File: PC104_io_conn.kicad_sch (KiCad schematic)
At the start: 14 parts, among them J13 ESQ-126-39-G-D_SAI, J15 ESQ-126-39-G-D_SAI

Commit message: A bunch of work on component selections
And little fixups for things I found.

Signed-off-by: Corey Minyard <corey@minyard.net>
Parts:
- C114, C133: value 10uF 10v -> 10uF 10V
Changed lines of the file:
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@@
 			)
 		)
-		(property "Value" "10uF 10v"
+		(property "Value" "10uF 10V"
 			(at 168.529 185.293 0)
 			(effects
@@
 			)
 		)
-		(property "Value" "10uF 10v"
+		(property "Value" "10uF 10V"
 			(at 88.011 162.433 0)
 			(effects

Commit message: More minor part number updates
Signed-off-by: Corey Minyard <corey@minyard.net>
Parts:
- J13, J15: value ESQ-126-39-G-D_SAI -> ESQ-126-39-G-D
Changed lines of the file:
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@@
 			)
 		)
-		(property "Value" "ESQ-126-39-G-D_SAI"
+		(property "Value" "ESQ-126-39-G-D"
 			(at 144.78 92.71 0)
 			(effects
@@
 			)
 		)
-		(property "Value" "ESQ-126-39-G-D_SAI"
+		(property "Value" "ESQ-126-39-G-D"
 			(at 248.92 92.71 0)
 			(effects

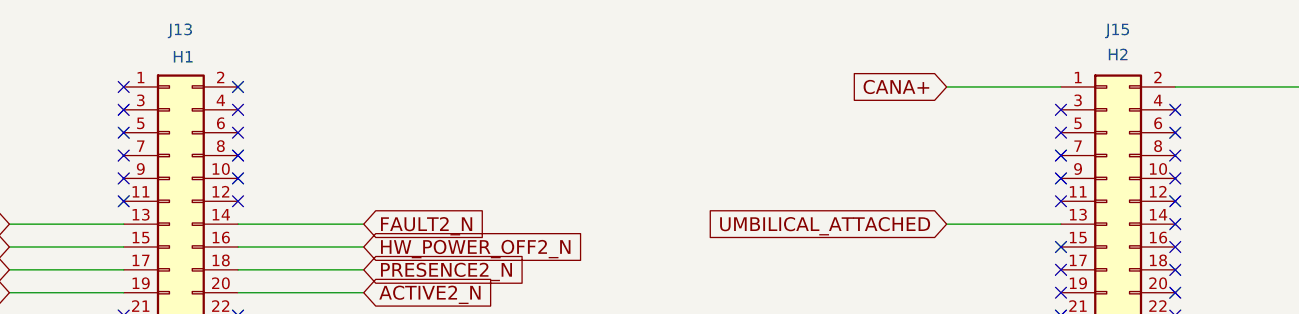
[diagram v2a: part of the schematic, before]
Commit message: Renumber shields and PC104 sockets
Separate out shields into their own designator category.

Make the PC104 sockets J1 and J2 to make it easier to move to other
boards.

Signed-off-by: Corey Minyard <corey@minyard.net>
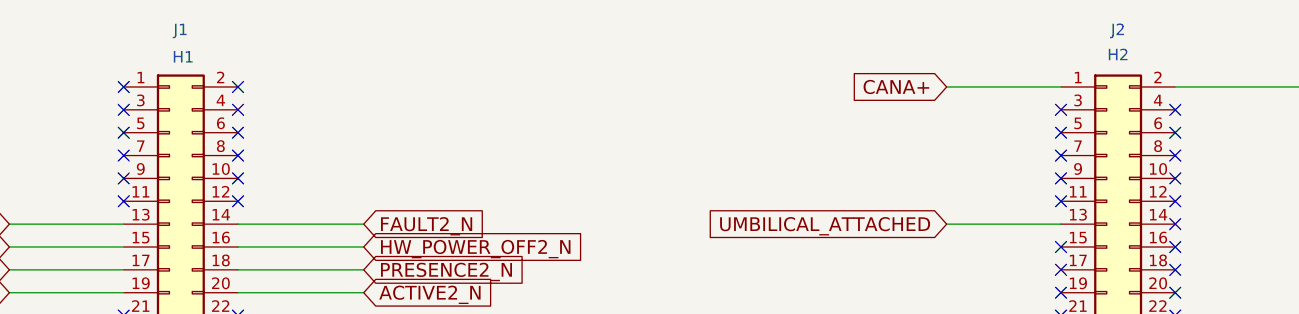
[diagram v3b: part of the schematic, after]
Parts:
- renumbered J13 to J1, J15 to J2
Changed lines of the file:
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@@
 		(on_board yes)
 		(dnp no)
-		(property "Reference" "J13"
+		(property "Reference" "J1"
 			(at 144.78 90.17 0)
 			(effects
@@
 			(project ""
 				(path "/cc9f42d2-6985-41ac-acab-5ab7b01c5b38/163b95be-82a7-4cd3-9077-48a01f79e25c"
-					(reference "J13")
+					(reference "J1")
 					(unit 1)
 				)
@@
 		(on_board yes)
 		(dnp no)
-		(property "Reference" "J15"
+		(property "Reference" "J2"
 			(at 248.92 90.17 0)
 			(effects
@@
 			(project "PacSat_AFSK"
 				(path "/cc9f42d2-6985-41ac-acab-5ab7b01c5b38/163b95be-82a7-4cd3-9077-48a01f79e25c"
-					(reference "J15")
+					(reference "J2")
 					(unit 1)
 				)

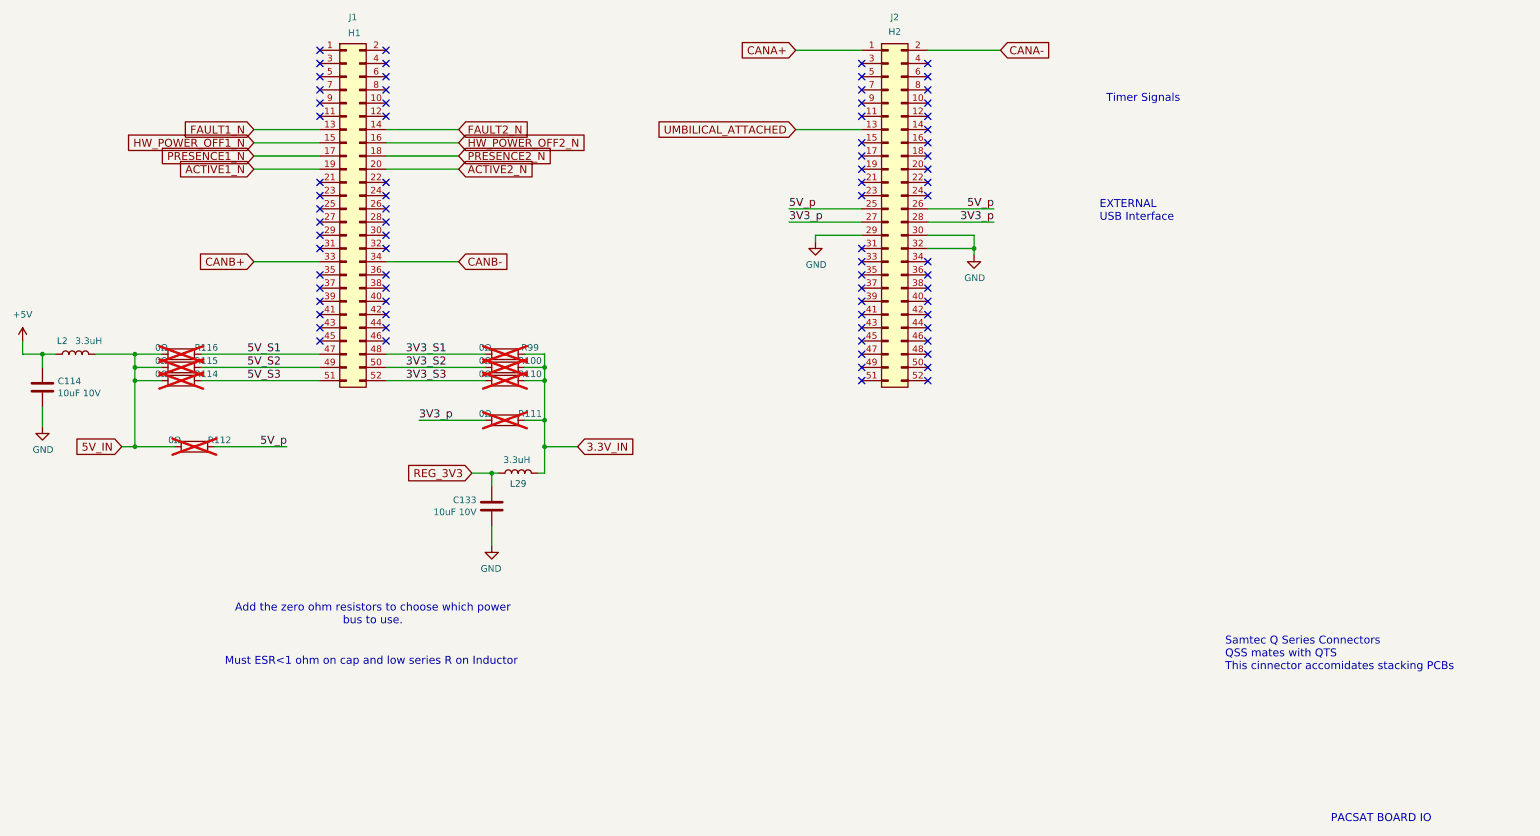
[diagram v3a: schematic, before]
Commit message: Rework the board to be the Fox Plus setup
Signed-off-by: Corey Minyard <corey@minyard.net>
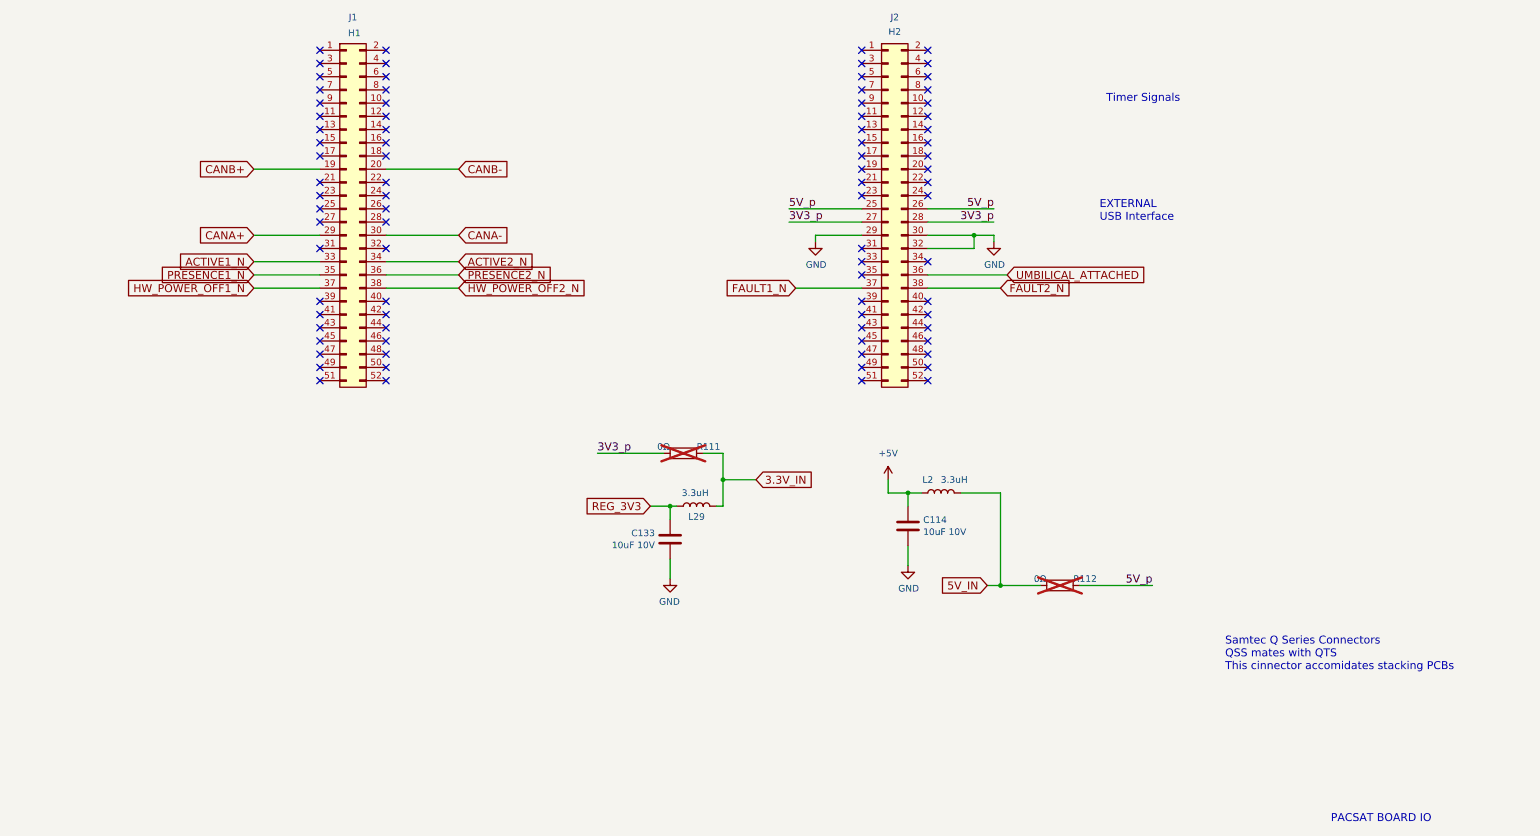
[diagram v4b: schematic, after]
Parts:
- removed R100, R110, R114, R115, R116, R99: 0Ω, Resistor_SMD:R_0603_1608Metric_Pad0.98x0.95mm_HandSolder, symbol Device:R
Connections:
- net ACTIVE1_N: now also J1.33 (Pin_33); no longer J1.19 (Pin_19)
- net ACTIVE2_N: now also J1.34 (Pin_34); no longer J1.20 (Pin_20)
- net CANA+: now also J1.29 (Pin_29); no longer J2.1 (Pin_1)
- net CANA-: now also J1.30 (Pin_30); no longer J2.2 (Pin_2)
- net CANB+: now also J1.19 (Pin_19); no longer J1.33 (Pin_33)
- net CANB-: now also J1.20 (Pin_20); no longer J1.34 (Pin_34)
- net FAULT1_N: now also J2.37 (Pin_37); no longer J1.13 (Pin_13)
- net FAULT2_N: now also J2.38 (Pin_38); no longer J1.14 (Pin_14)
- net HW_POWER_OFF1_N: now also J1.37 (Pin_37); no longer J1.15 (Pin_15)
- net HW_POWER_OFF2_N: now also J1.38 (Pin_38); no longer J1.16 (Pin_16)
- net PRESENCE1_N: now also J1.35 (Pin_35); no longer J1.17 (Pin_17)
- net PRESENCE2_N: now also J1.36 (Pin_36); no longer J1.18 (Pin_18)
- net UMBILICAL_ATTACHED: now also J2.36 (Pin_36); no longer J2.13 (Pin_13)
- net 3V3_S1: no longer names the net of J1.48 (Pin_48)
- net 3V3_S2: no longer names the net of J1.50 (Pin_50)
- net 3V3_S3: no longer names the net of J1.52 (Pin_52)
- net 5V_S1: no longer names the net of J1.47 (Pin_47)
- net 5V_S2: no longer names the net of J1.49 (Pin_49)
- net 5V_S3: no longer names the net of J1.51 (Pin_51)
- no-connect marks 78 -> 84
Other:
- note removed: "Add the zero ohm resistors to choose which power bus to use."
- note removed: "Must ESR<1 ohm on cap and low series R on Inductor"
- moved on the sheet: C114, C133, L2, L29, R111, R112

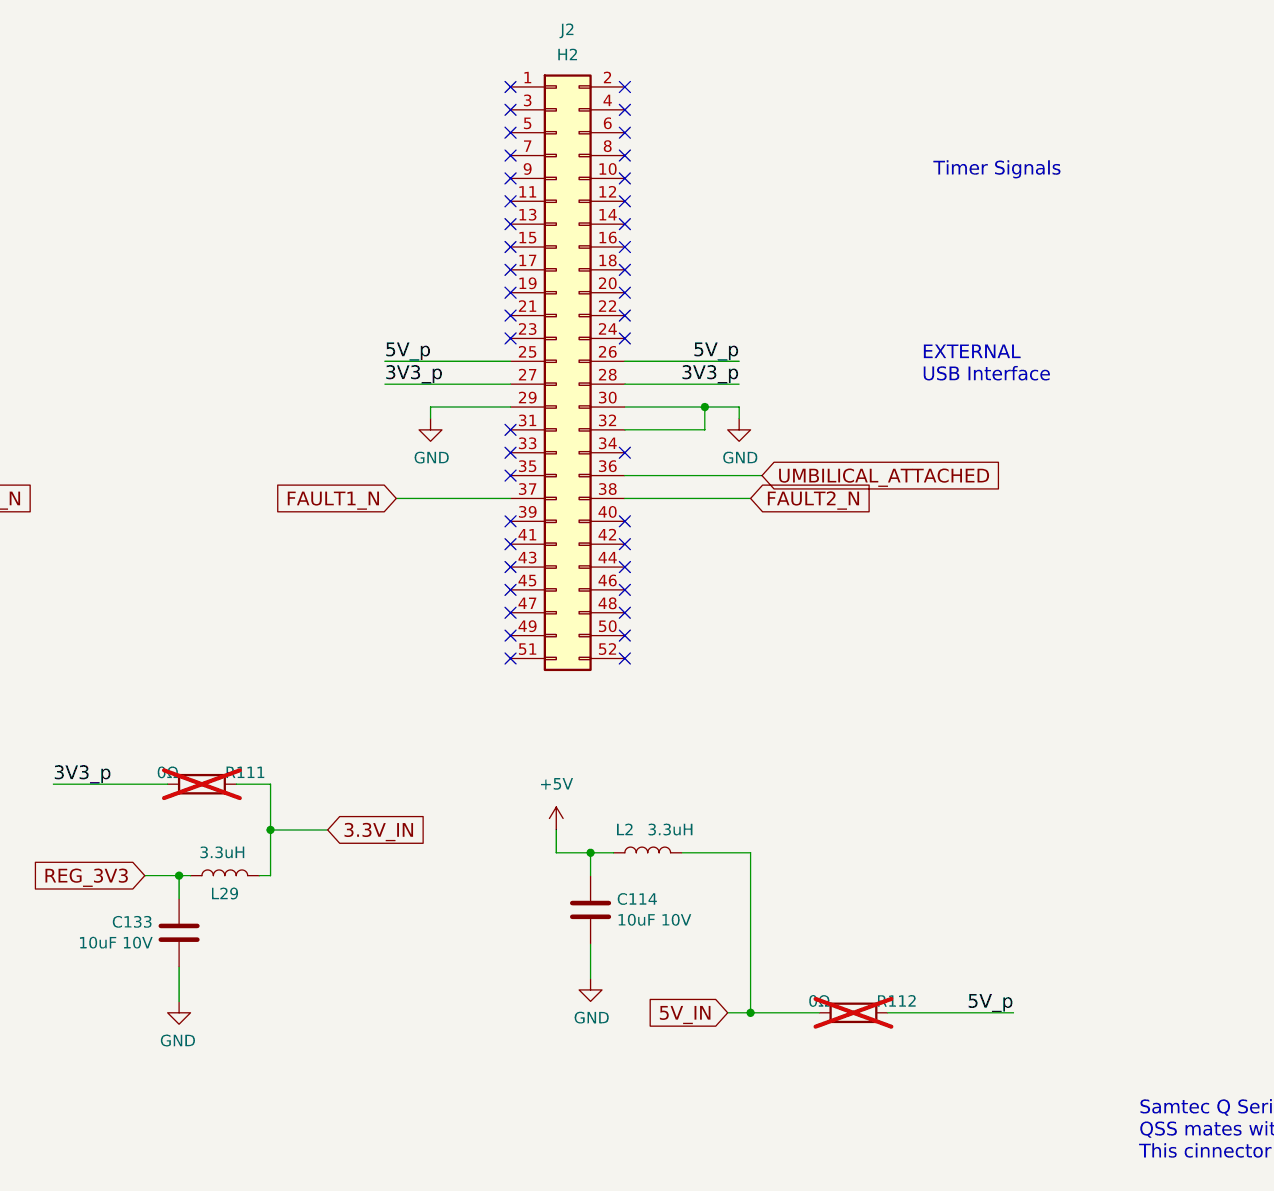
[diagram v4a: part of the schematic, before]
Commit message: More minor cleanups
Tune the CAN bus lines.

Clean up some tracks.

Signed-off-by: Corey Minyard <corey@minyard.net>
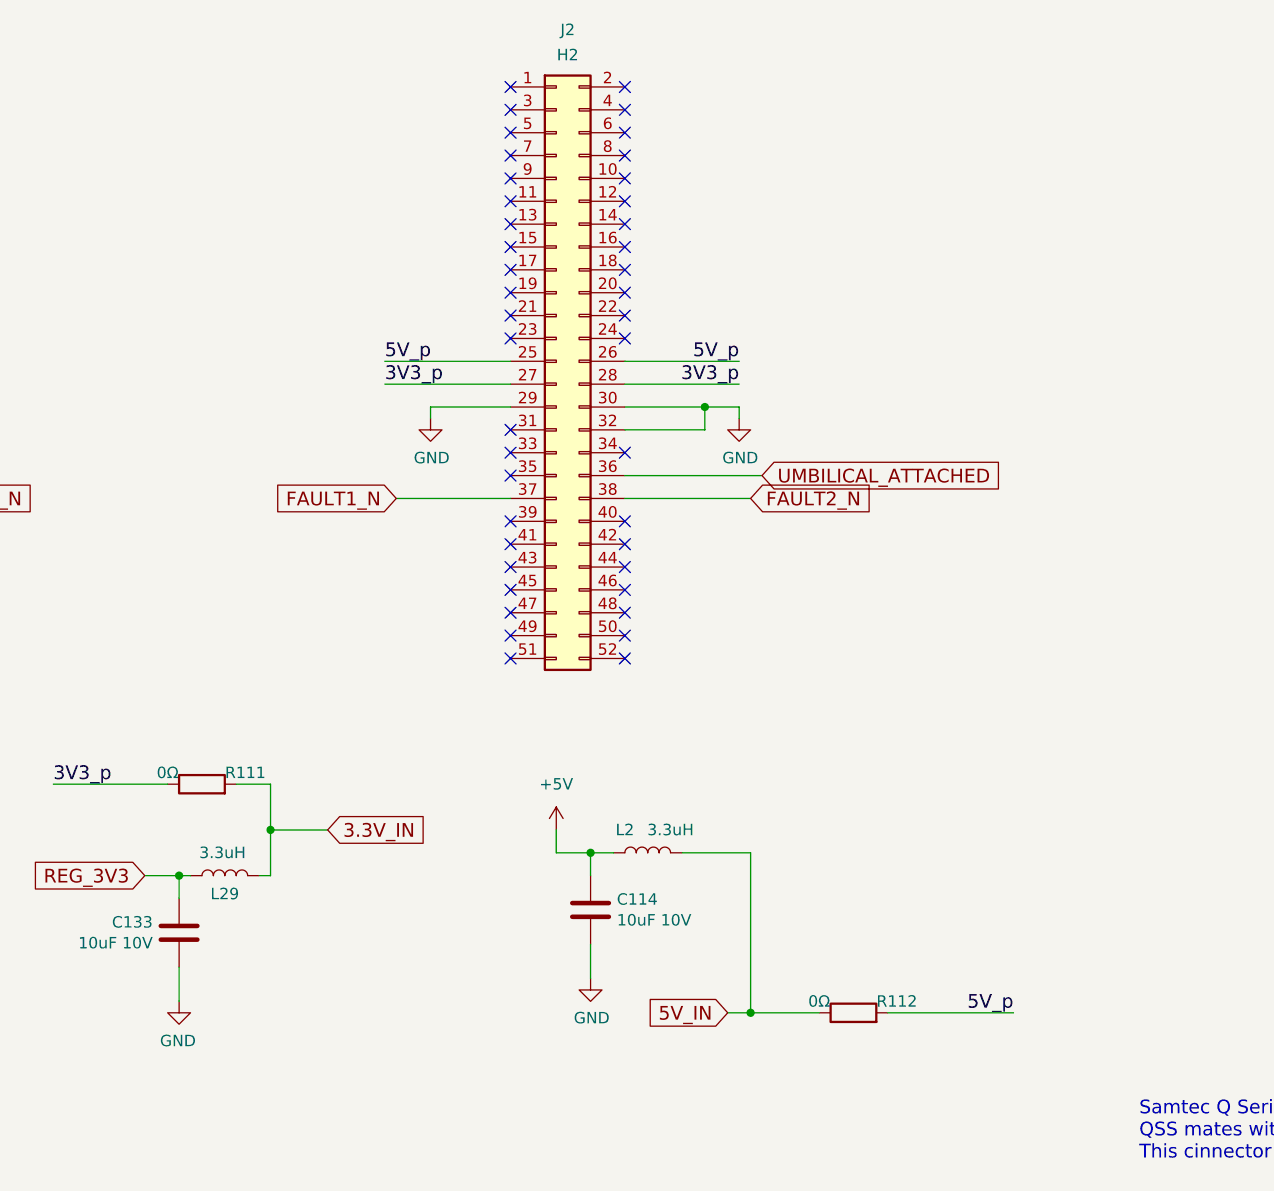
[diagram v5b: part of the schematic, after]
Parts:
- R111, R112: now fitted; now in the parts list
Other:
- note removed: "EXTERNAL USB Interface"
- note removed: "Timer Signals"
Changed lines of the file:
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@@
-		)
-	)
-	(text "Timer Signals"
-		(exclude_from_sim no)
-		(at 289.56 106.68 0)
-		(effects
-			(font
-				(size 1.524 1.524)
-			)
-			(justify left bottom)
 		)
 	)
@@
 		(exclude_from_sim no)
 		(at 332.74 245.11 0)
-		(effects
-			(font
-				(size 1.524 1.524)
-			)
-			(justify left bottom)
-		)
-	)
-	(text "EXTERNAL\nUSB Interface"
-		(exclude_from_sim no)
-		(at 288.29 129.54 0)
 		(effects
 			(font
@@
 		(unit 1)
 		(exclude_from_sim no)
-		(in_bom no)
+		(in_bom yes)
 		(on_board yes)
-		(dnp yes)
+		(dnp no)
 		(property "Reference" "R111"
 			(at 213.106 172.72 90)
@@
 		(unit 1)
 		(exclude_from_sim no)
-		(in_bom no)
+		(in_bom yes)
 		(on_board yes)
-		(dnp yes)
+		(dnp no)
 		(property "Reference" "R112"
 			(at 285.496 198.12 90)

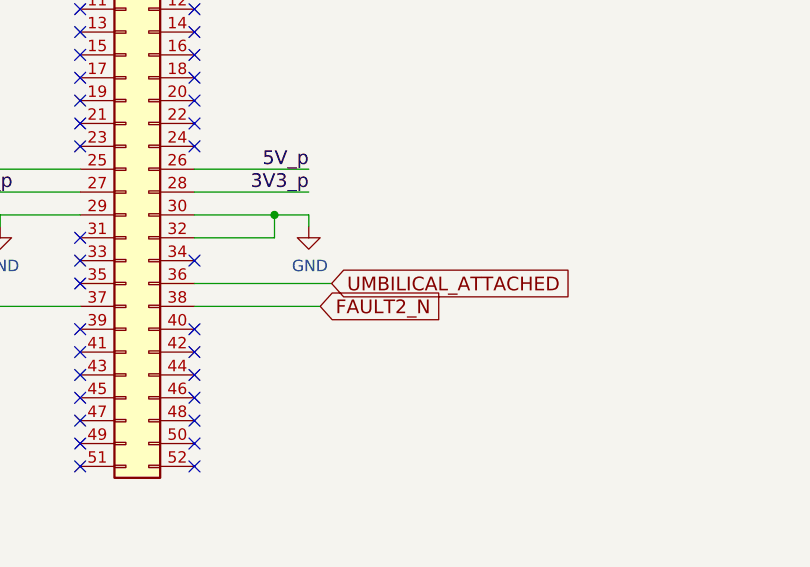
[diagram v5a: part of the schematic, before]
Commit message: Move to two smaller shields for the TX section
Signed-off-by: Corey Minyard <corey@minyard.net>
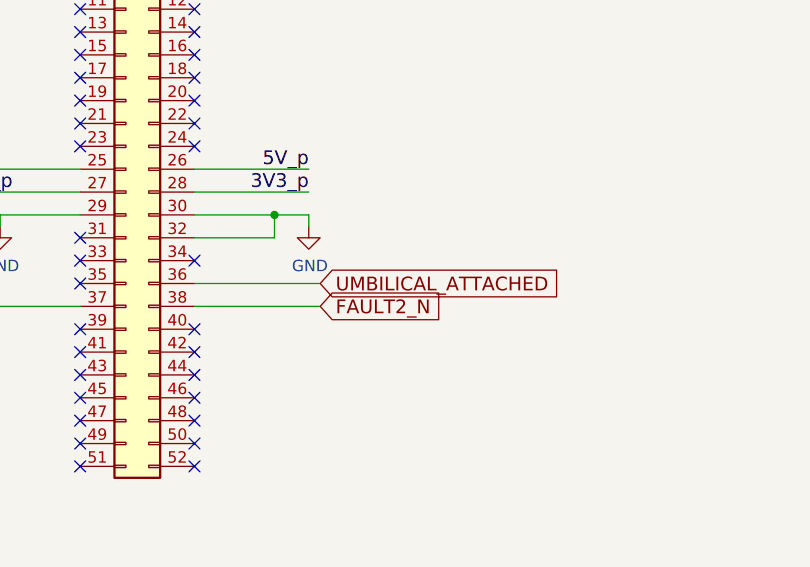
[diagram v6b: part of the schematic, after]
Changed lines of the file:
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@@
 	(wire
 		(pts
-			(xy 255.27 139.7) (xy 270.51 139.7)
+			(xy 255.27 139.7) (xy 269.24 139.7)
 		)
 		(stroke
@@
 	(global_label "UMBILICAL_ATTACHED"
 		(shape input)
-		(at 270.51 139.7 0)
+		(at 269.24 139.7 0)
 		(fields_autoplaced yes)
 		(effects
@@
 		)
 		(property "Intersheetrefs" "${INTERSHEET_REFS}"
-			(at 297.0376 139.7 0)
-			(effects
-				(font
+			(at 295.7676 139.7 0)
+			(effects
+				(font
